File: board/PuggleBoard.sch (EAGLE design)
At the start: 146 parts, among them U1 OPA4209, U10 24C, U2 ADS8331, U3 AD5686, U4 OPA4209, U5 LM2663, U6 TPS7A3001, U7 TPS7A4901, U8 REF5040, U9 AD8032

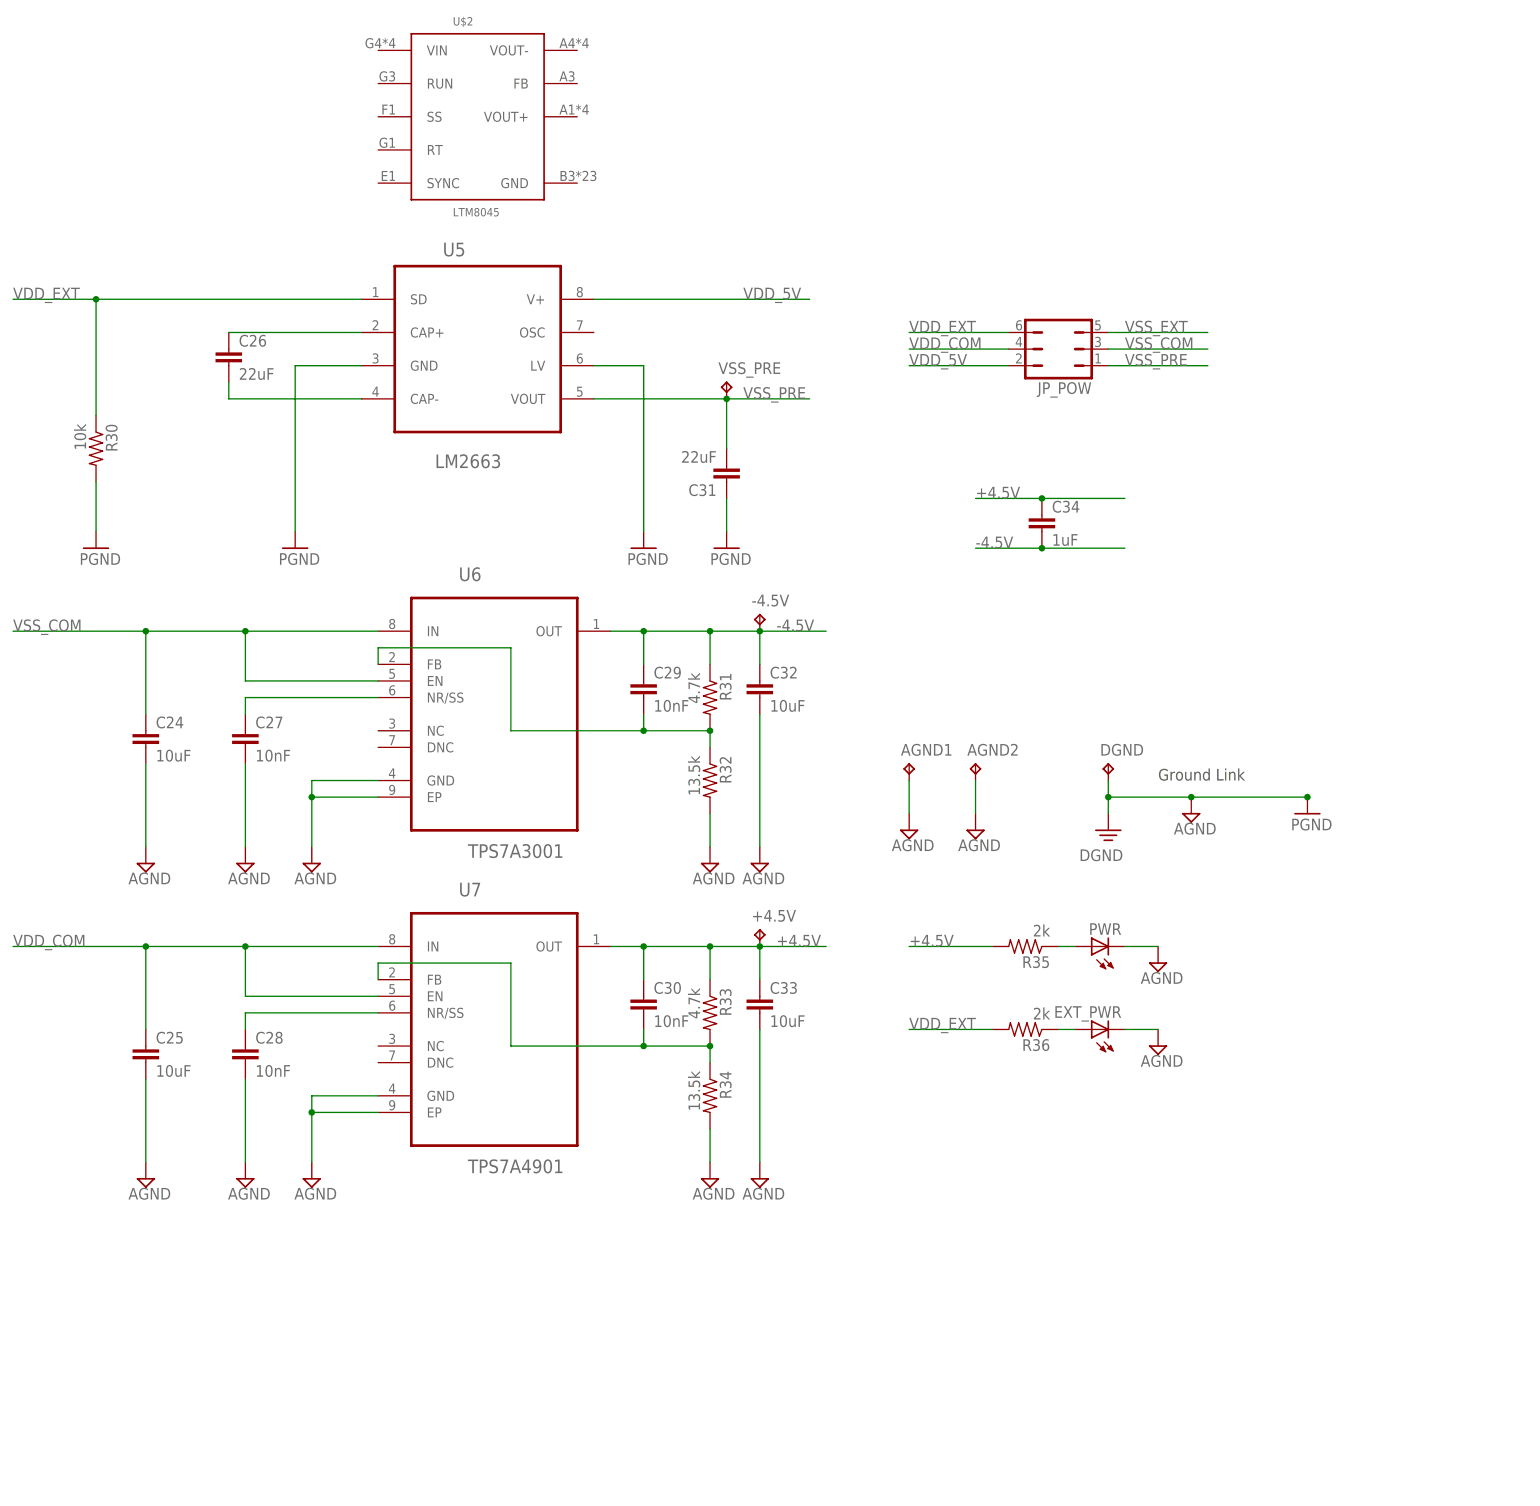
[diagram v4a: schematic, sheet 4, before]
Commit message: Replaced swiching inverter with uModule. Removed external power option.
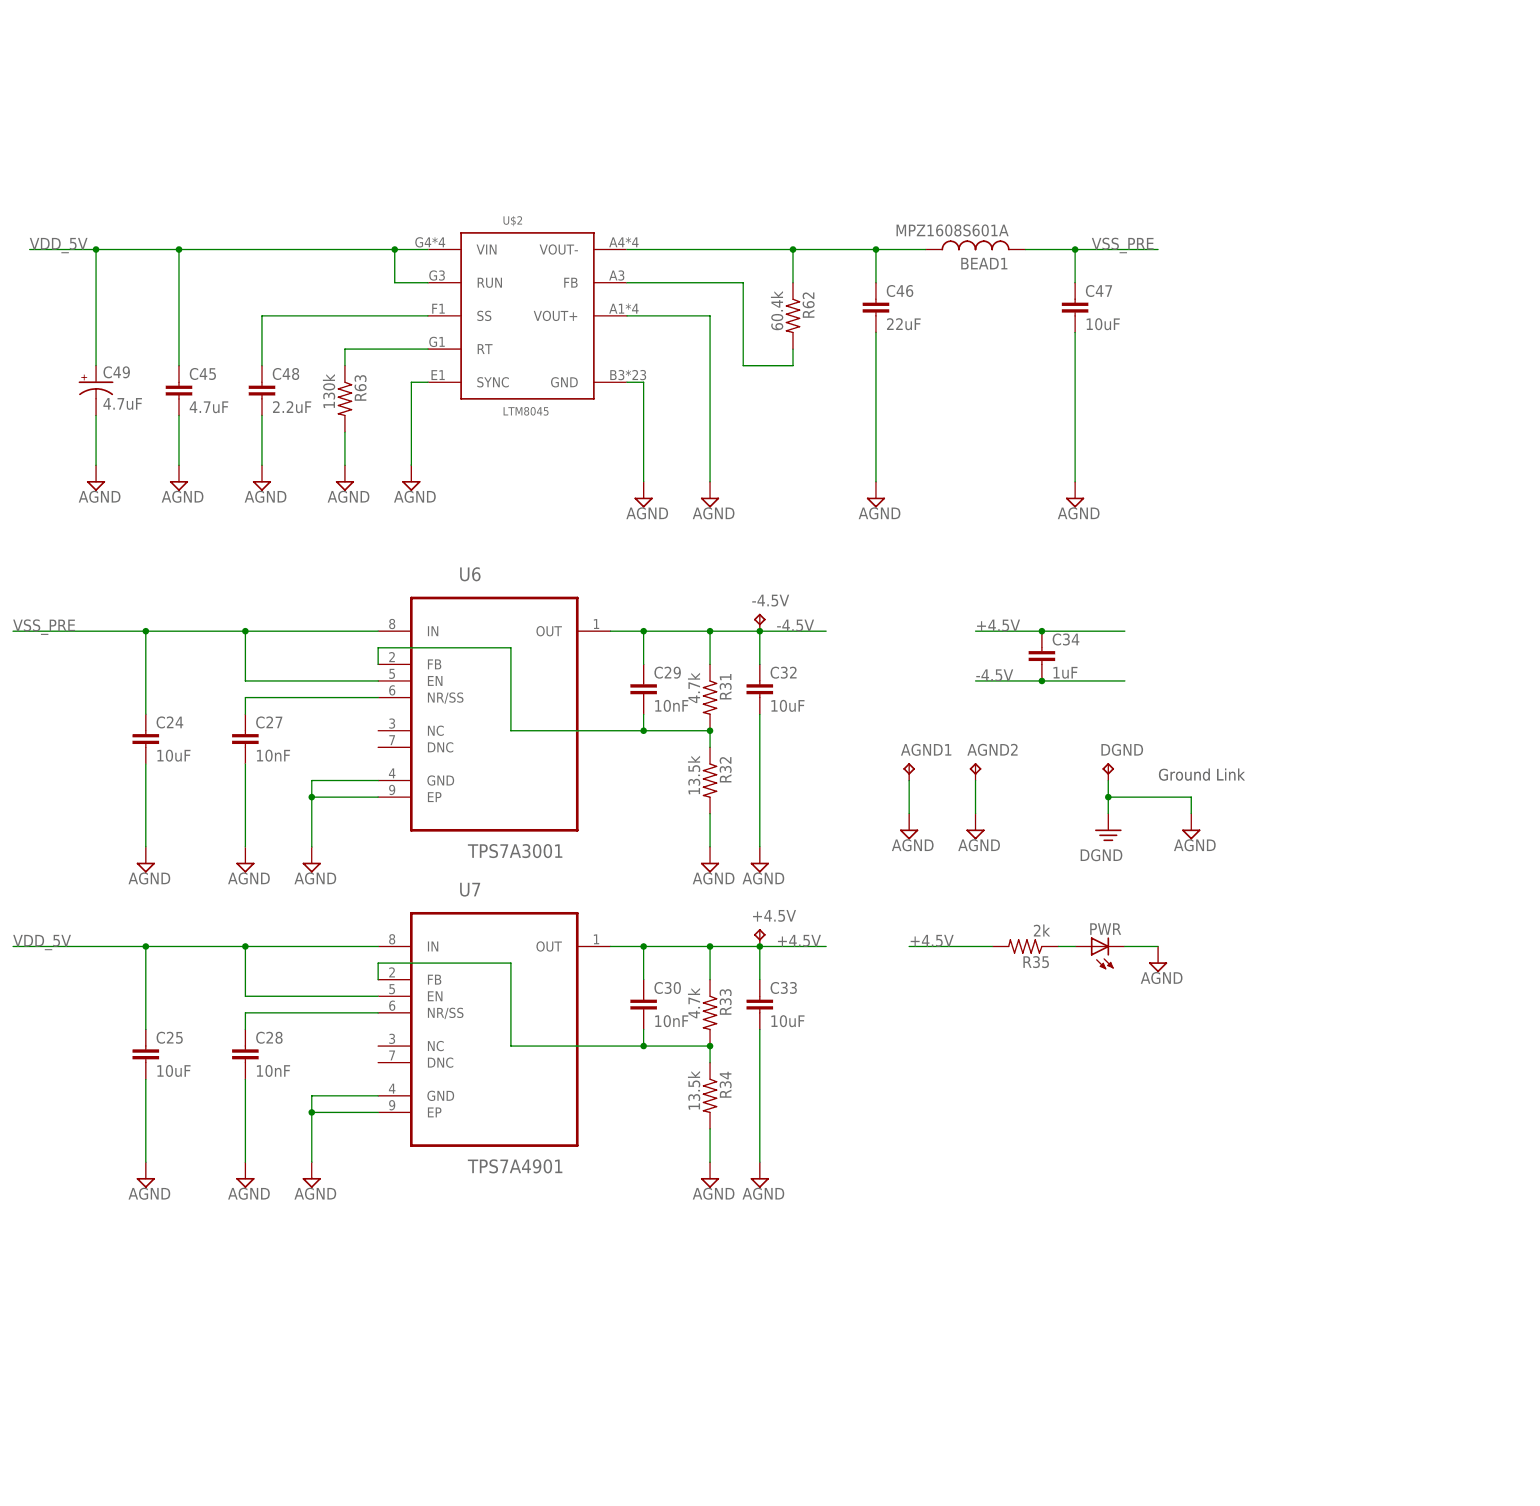
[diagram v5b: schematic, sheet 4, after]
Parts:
- removed C26, C31: 22uF, resistor:C-EUC1206
- removed EXT_PWR: (no value), led:LEDCHIPLED_0805
- removed JP_POW: (no value), jumper:JP3Q
- removed PWR_EXT: (no value), adafruit:PINHD-1X3
- removed R30: 10k, rcl:R-US_R0603
- removed R36: 2k, rcl:R-US_R0603
- removed U5: LM2663, ti-extended:LM2663
- removed VSS_PRE: TPB1,27, testpad:TPB1,27
- added BEAD1: MPZ1608S601A, rcl:L-USL0603
- added C45: 4.7uF, rcl:C-EUC0805
- added C46: 22uF, resistor:C-EUC1206
- added C47: 10uF, rcl:C-EUC0805
- added C48: 2.2uF, resistor:C-EUC1206
- added C49: 4.7uF, rcl:CPOL-USA
- added R62: 60.4k, rcl:R-US_R0603
- added R63: 130k, rcl:R-US_R0603
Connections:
- removed net N$33: C26.1, U5.CAP+
- removed net N$34: C26.2, U5.CAP-
- removed net N$7: EXT_PWR.A, R36.1
- removed net PGND: C31.1, R30.2, U5.GND, U5.LV
- removed net VDD_COM: C25.1, JP_POW.4, U7.EN, U7.IN
- removed net VDD_EXT: JP_POW.6, PWR_EXT.1, R30.1, R36.2, U5.SD
- removed net VSS_COM: C24.1, JP_POW.3, U6.EN, U6.IN
- removed net VSS_EXT: JP_POW.5, PWR_EXT.3
- new net N$37: R63.1, U$2.RT
- new net N$38: U$2.SYNC
- new net N$39: C48.1, U$2.SS
- new net N$45: R62.2, U$2.FB
- new net VOUT-: BEAD1.1, C46.1, R62.1, U$2.VOUT-
- net AGND: now also C45.2, C46.2, C47.2, C48.2, C49.-, R63.2, U$2.GND, U$2.VOUT+; no longer EXT_PWR.C, PWR_EXT.2
- net VDD_5V: now also C25.1, C45.1, C49.+, U$2.RUN, U$2.VIN, U7.EN, U7.IN; no longer JP_POW.2, U5.V+
- net VSS_PRE: now also BEAD1.2, C24.1, C47.1, U6.EN, U6.IN; no longer C31.2, JP_POW.1, U5.VOUT, VSS_PRE.TP
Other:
- moved on the sheet: C34, RESET, U$2

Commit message: More layout.
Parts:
- R35: value 2k -> 1k
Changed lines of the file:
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@@
 <part name="+4.5V" library="testpad" deviceset="TP" device="PAD1-17" value="TPPAD1-17"/>
 <part name="DGND6" library="supply2" deviceset="PE" device="" value="DGND"/>
-<part name="R35" library="rcl" deviceset="R-US_" device="R0603" value="2k"/>
+<part name="R35" library="rcl" deviceset="R-US_" device="R0603" value="1k"/>
 <part name="PWR" library="led" deviceset="LED" device="CHIPLED_0805"/>
 <part name="SUPPLY32" library="supply2" deviceset="AGND" device=""/>

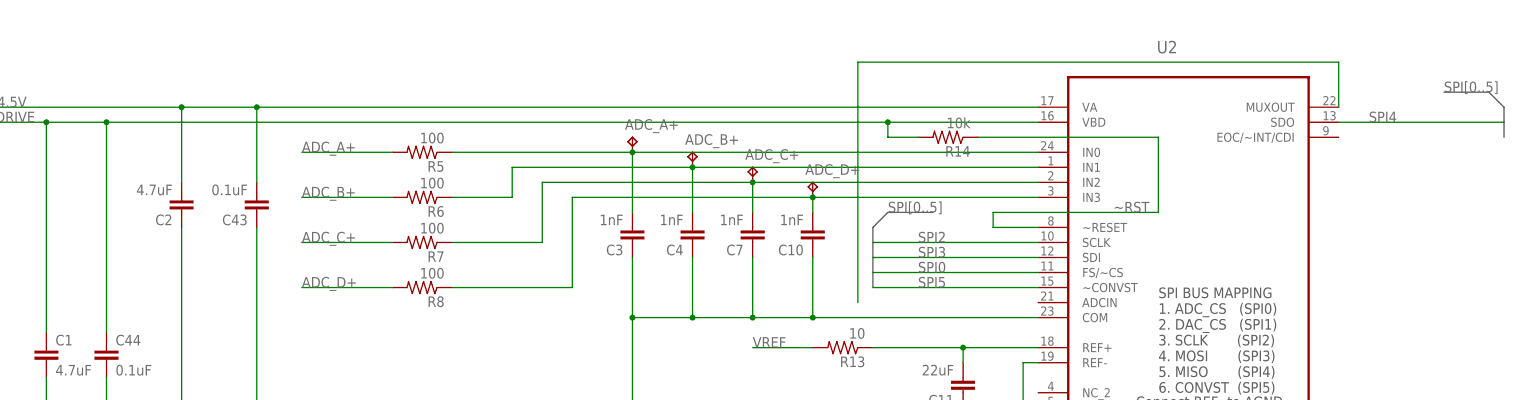
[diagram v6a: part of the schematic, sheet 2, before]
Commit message: Still have split ground planes, but they are all reffered to as GND now, since they have a link-point near the ADC.
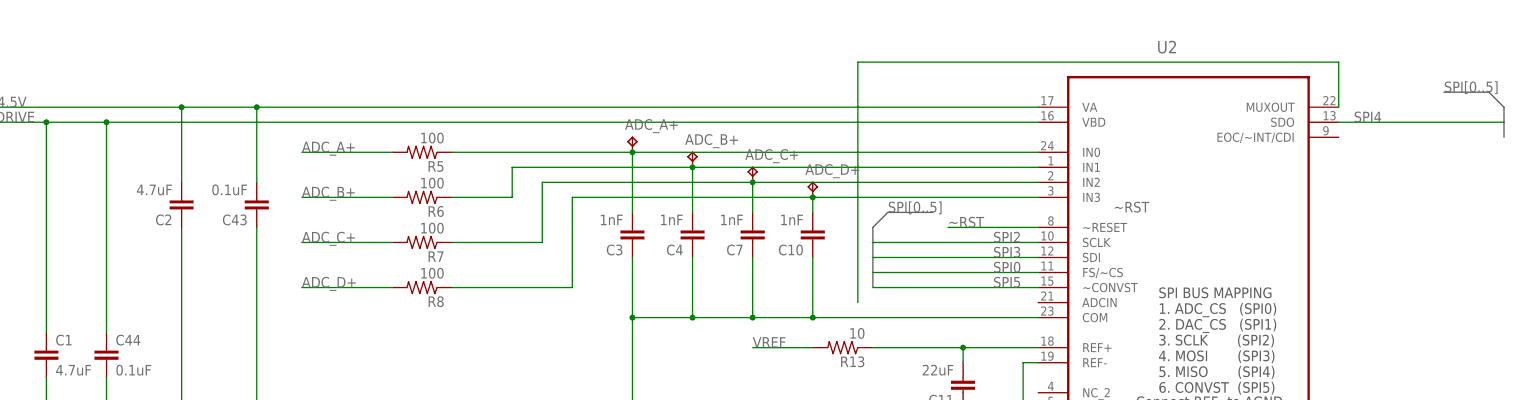
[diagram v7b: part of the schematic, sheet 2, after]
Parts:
- removed AGND2: TPPAD1-17, testpad:TPPAD1-17
- removed C34: 1uF, rcl:C-EUC0603
- removed R14: 10k, rcl:R-US_R0603
- renumbered AGND1 to AGND
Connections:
- new net SPI0: R55.1, U2.FS/~CS
- new net SPI3: R47.2, U2.SDI, U3.SDIN
- new net SPI4: R46.2, U2.SDO, U3.SDO
- net +4.5V: no longer C34.1, R35.2
- net -4.5V: no longer C34.2
- net AGND: no longer AGND2.TP
- net SPI1: now also R60.1, U3.SYNC*; no longer R48.2, R55.1
- net SPI2: now also R48.2, U2.SCLK, U3.SCLK; no longer R46.2, R47.2
- net SPI5: now also R54.1, U2.~CONVST; no longer R60.1
- net VDD_5V: now also R35.2
- net VDRIVE: no longer R14.2
- net ~RST: no longer R14.1

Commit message: Nearly done with split-plane version.
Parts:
- BB1: value BEAGLEBONE_OUTLINE -> BEAGLEBONE_OUTLINEPUGGLEBOARD; device adafruit:BEAGLEBONE_OUTLINE -> puggleboard:BEAGLEBONE_OUTLINEPUGGLEBOARD
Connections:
- removed net AGND: AGND.TP, A_I/O.1, A_I/O.2, C1.2, C10.1, C11.1, C12.2, C13.2, C15.2, C16.2, C17.2, C18.2, C19.2, C2.1, C20.2, C21.2, C22.2, C23.2, C24.2, C25.2, C27.2, C28.2, C3.1, C32.2, C33.2, C35.2, C36.1, C37.2, C38.1, C39.2, C4.1, C40.2, C41.2, C43.1, C44.2, C45.2, C46.2, C47.2, C48.2, C49.-, C5.2, C6.2, C7.1, C8.2, C9.2, PWR.C, R26.1, R27.1, R28.1, R29.1, R32.2, R34.2, R37.A, R63.2, U$2.GND, U$2.VOUT+, U2.AGND, U2.COM, U2.DGND, U2.REF-, U3.GND, U6.EP, U6.GND, U7.EP, U7.GND, U8.GND, U9.-VS
- removed net DGND: BB1.GND@7, BB1.GND@8, C14.2, C42.2, DGND.TP, RESET.S, RESET.S1, S1.1, S1.2, U$1.CLOCKSHIELD, U$1.DATA0SHIELD, U$1.DATA1SHIELD, U$1.DATA2SHIELD, U10.GND, U3.GAIN
- new net GND: AGND.TP, A_I/O.1, A_I/O.2, BB1.GND@7, BB1.GND@8, C1.2, C10.1, C11.1, C12.2, C13.2, C14.2, C15.2, C16.2, C17.2, C18.2, C19.2, C2.1, C20.2, C21.2, C22.2, C23.2, C24.2, C25.2, C27.2, C28.2, C3.1, C32.2, C33.2, C35.2, C36.1, C37.2, C38.1, C39.2, C4.1, C40.2, C41.2, C42.2, C43.1, C44.2, C45.2, C46.2, C47.2, C48.2, C49.-, C5.2, C6.2, C7.1, C8.2, C9.2, DGND.TP, PWR.C, R26.1, R27.1, R28.1, R29.1, R32.2, R34.2, R37.A, R63.2, RESET.S, RESET.S1, S1.1, S1.2, U$1.CLOCKSHIELD, U$1.DATA0SHIELD, U$1.DATA1SHIELD, U$1.DATA2SHIELD, U$2.GND, U$2.VOUT+, U10.GND, U2.AGND, U2.COM, U2.DGND, U2.REF-, U3.GAIN, U3.GND, U6.EP, U6.GND, U7.EP, U7.GND, U8.GND, U9.-VS
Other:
- note added: "2.0"
- moved on the sheet: ADC_A+, ADC_B+, ADC_C+, ADC_D+, C1, C10, C11, C15, C16, C17, C18, C19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
